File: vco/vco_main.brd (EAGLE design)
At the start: 94.9 x 107.9 mm, 82 parts, among them IC1 OPA4130U, IC2 LM13700M, IC3 OPA4130U, IC4 OPA4130U, Q1 MMBFJ3

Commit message: added gerbers
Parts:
- added C10, C11, C12, C13, C14, C15, C16, C17, C18, C19, C8, C9: 1n, dan:C0603
- moved R13 12.0 mm to (15.2, 95.2)
- moved U$2 5.08 mm to (8.89, 49.5)
- moved Q1 2.84 mm to (87.6, 76.2)
- moved C1 1.27 mm to (15.2, 85.1), turned to 270 degrees
- moved R1 1.27 mm to (12.7, 85.1), turned to 90 degrees
- moved U$5 1.27 mm to (86.4, 97.8)
- turned C7 to 270 degrees
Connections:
- net +12V: now also C14.1, C15.1, C16.1, C17.1, C18.1, C19.1, IC2.11, POWER.10, POWER.9
- net -12V: now also C10.1, C11.1, C12.1, C13.1, C8.1, C9.1, IC2.6, POWER.1, POWER.2
- net GND: now also C10.2, C11.2, C12.2, C13.2, C14.2, C15.2, C16.2, C17.2, C18.2, C19.2, C8.2, C9.2, POWER.3, POWER.4, POWER.5, POWER.6, POWER.7, POWER.8
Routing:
- net -12V: track 0.00 -> 289.4 mm, vias 0 -> 21
- net +12V: track 0.00 -> 244.0 mm, vias 0 -> 18
- net SYNC: track 0.00 -> 228.2 mm, vias 0 -> 13
- net N$5: track 2.54 -> 185.8 mm, vias 0 -> 18
- net TRI: track 2.54 -> 163.4 mm, vias 0 -> 15
- net N$12: track 0.00 -> 145.1 mm, vias 0 -> 11
- net N$4: track 0.00 -> 138.5 mm, vias 0 -> 12
- net N$36: track 0.00 -> 128.6 mm, vias 0 -> 7
- net N$50: track 0.00 -> 120.6 mm, vias 0 -> 7
- net N$9: track 0.00 -> 118.5 mm, vias 0 -> 8
- net N$19: track 0.00 -> 112.2 mm, vias 0 -> 5
- net N$3: track 0.00 -> 107.4 mm, vias 0 -> 12
- net N$45: track 0.00 -> 103.5 mm, vias 0 -> 5
- net N$24: track 0.00 -> 102.9 mm, vias 0 -> 5
- net N$51: track 0.00 -> 83.0 mm, vias 0 -> 6
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- added copper zone on layer 16, net GND
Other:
- board size 94.9 x 107.9 mm -> 94.9 x 108 mm
- board text added: "tempco"

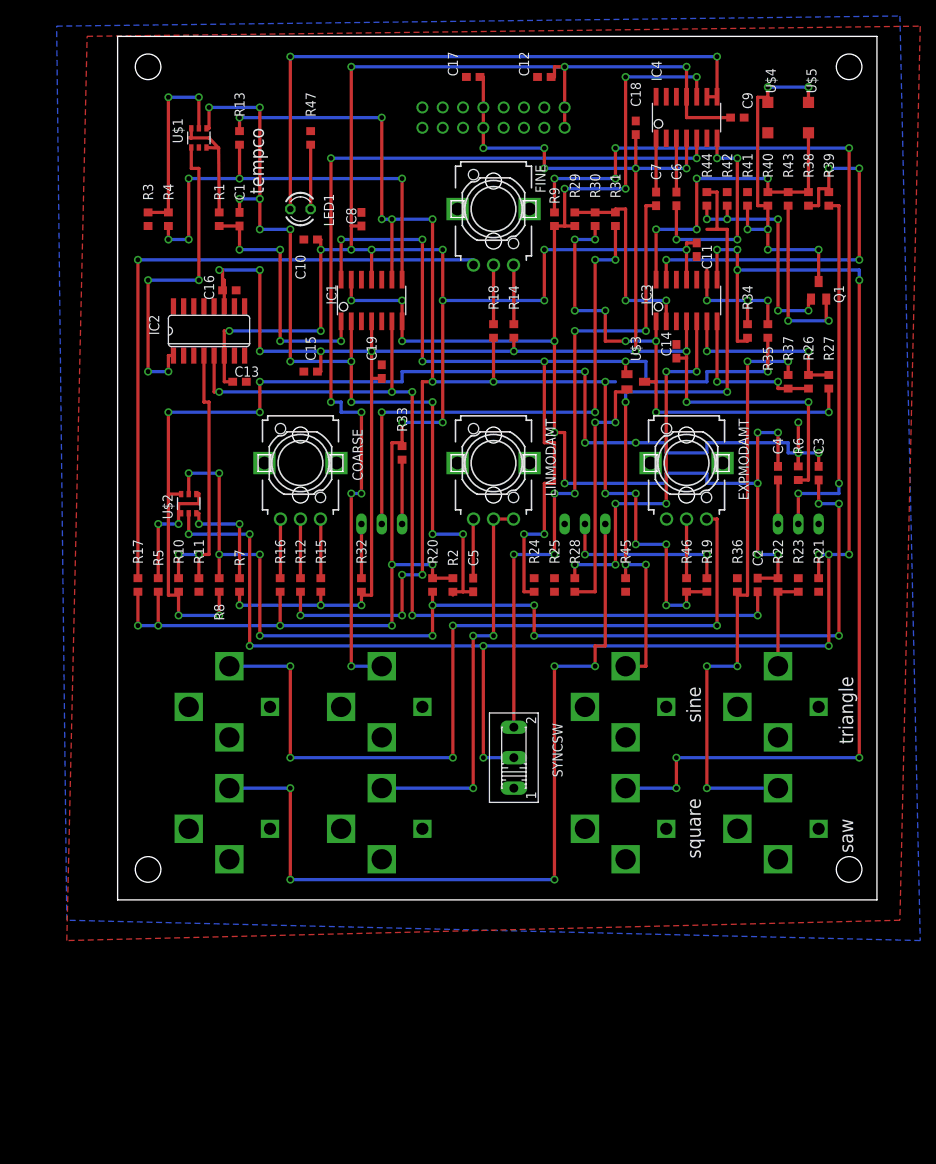
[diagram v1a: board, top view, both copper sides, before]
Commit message: fixed the schematic.  need to check polarity on current source and square comparator.  moved most of the labels to the silkscreen layer, but need to do that with the new components.
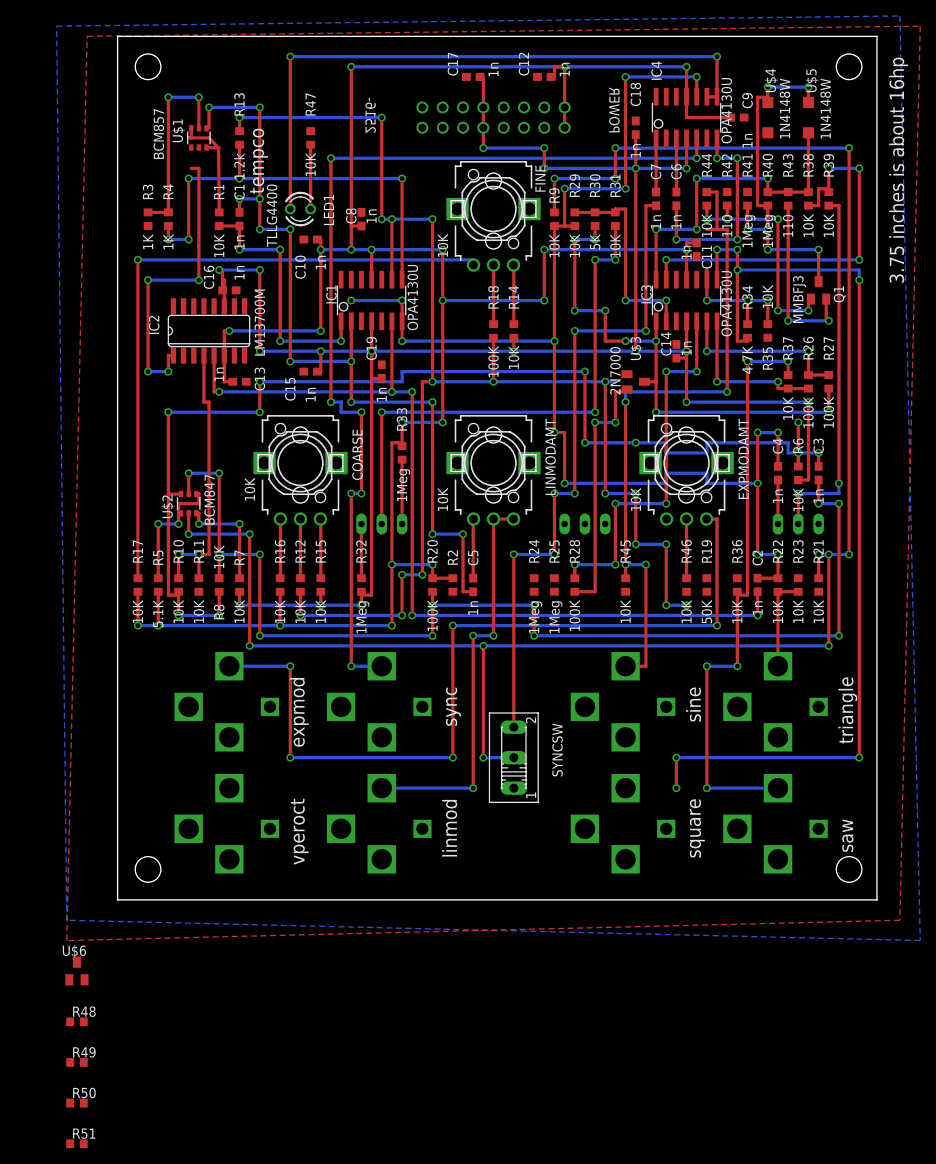
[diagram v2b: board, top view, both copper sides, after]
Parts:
- added R48: 4.7K, dan:R0603
- added R49, R50, R51: 10K, dan:R0603
- added U$6: MMBT3904, dan:SOT23
- R13: value 10K -> 1.2k
- R18, R26, R27, R28: value 10K -> 100K
- R19: value 10K -> 50K
- R2: value (none) -> 1Meg
- R3, R4: value 10K -> 1K
- R30: value 10K -> 5K
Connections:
- removed net IABC1: IC2.1, U$1.4
- new net IABC: IC2.1, U$1.1
- new net N$54: IC4.12, VPEROCT.P$3
- new net N$55: IC4.13, IC4.14, SCALE.E
- new net N$56: SCALE.S, U$6.1
- new net N$58: R51.1
- new net N$9: R49.2, R50.1, SQUARE.P$3
- net +12V: now also U$6.3
- net -12V: now also R48.1
- net GND: now also IC1.13, R50.2; no longer IC1.12, LINMOD.P$2
- net N$22: now also R48.2, U$6.2; no longer SCALE.S
- net N$24: now also R2.2, U$1.4; no longer SCALE.E, VPEROCT.P$3
- net N$3: no longer R2.2, U$1.1
- net N$36: now also R49.1; no longer SQUARE.P$3
- net TRI: now also IC1.12, R51.2; no longer IC1.13
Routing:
- net N$57: track 118.5 -> 0.00 mm, vias 8 -> 0
- net N$24: track 102.9 -> 0.00 mm, vias 5 -> 0
- net IABC1: track 40.5 -> 0.00 mm, vias 4 -> 0
- net IABC: track 0.00 -> 37.9 mm, vias 0 -> 4
- net N$22: track 22.0 -> 0.00 mm, vias 2 -> 0
- net N$36: track 128.6 -> 122.3 mm
- net N$5: track 185.8 -> 181.5 mm
- net TRI: track 163.4 -> 160.8 mm
- net N$3: track 107.4 -> 105.4 mm

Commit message: fixed schematic.  moved all labels to silkscreen.  fixed layout.  need to make gerbers.
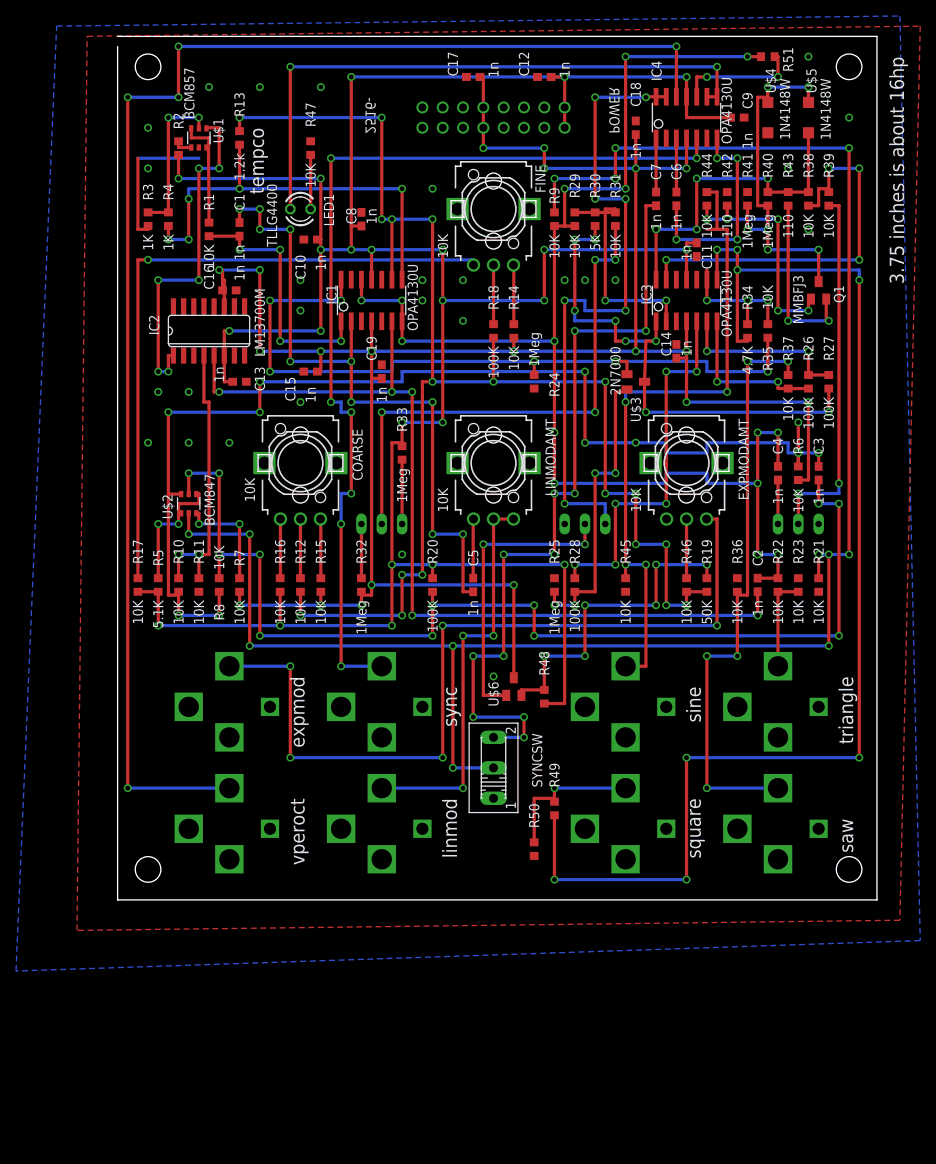
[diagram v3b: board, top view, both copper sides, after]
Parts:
- moved R51 161.0 mm to (81.3, 105.4)
- moved R48 71.2 mm to (53.3, 25.4), turned to 90 degrees
- moved R49 67.6 mm to (54.6, 11.4), turned to 90 degrees
- moved R50 65.4 mm to (52.1, 6.35), turned to 270 degrees
- moved U$6 65.2 mm to (49.5, 26.7)
- moved R2 64.5 mm to (7.62, 94.0), turned to 90 degrees
- moved R24 25.4 mm to (52.1, 64.8), turned to 90 degrees
- moved SYNCSW 2.84 mm to (47.0, 16.5)
- moved R1 1.80 mm to (11.4, 83.8)
- moved C1 1.27 mm to (15.2, 83.8)
- moved R47 1.27 mm to (24.1, 94.0)
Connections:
- removed net N$58: R51.1
- new net N$59: IC4.10, R51.2
- net TRI: now also R51.1; no longer IC4.10, R51.2
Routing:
- net N$54: track 0.00 -> 180.3 mm, vias 0 -> 5
- net N$57: track 0.00 -> 94.1 mm, vias 0 -> 6
- net N$55: track 0.00 -> 81.3 mm, vias 0 -> 7
- net -12V: track 289.4 -> 342.3 mm, vias 21 -> 23
- net N$22: track 0.00 -> 41.2 mm, vias 0 -> 6
- net N$56: track 0.00 -> 37.0 mm, vias 0 -> 2
- net N$36: track 122.3 -> 157.0 mm, vias 7 -> 8
- net +12V: track 244.0 -> 273.3 mm, vias 18 -> 20
- net N$3: track 105.4 -> 83.8 mm, vias 12 -> 10
- net N$9: track 0.00 -> 19.0 mm, vias 0 -> 1
- net GND: track 0.00 -> 18.2 mm, vias 0 -> 27
- net N$51: track 83.0 -> 99.5 mm, vias 6 -> 11
- net N$59: track 0.00 -> 15.6 mm, vias 0 -> 2
- net TRI: track 160.8 -> 170.2 mm
- net N$10: track 31.8 -> 37.7 mm, vias 2 -> 4
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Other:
- board size 94.9 x 108 mm -> 94.9 x 107.9 mm

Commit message: fixed some drc errors.  made gerbers.  silkscreen gerber doesn't seem to be getting the fonts correctly.
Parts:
- added R52: 1Meg, dan:R0603
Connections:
- net GND: now also R52.1
- net N$54: now also R52.2
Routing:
- net GND: track 18.2 -> 8.04 mm
- net N$54: track 180.3 -> 185.4 mm

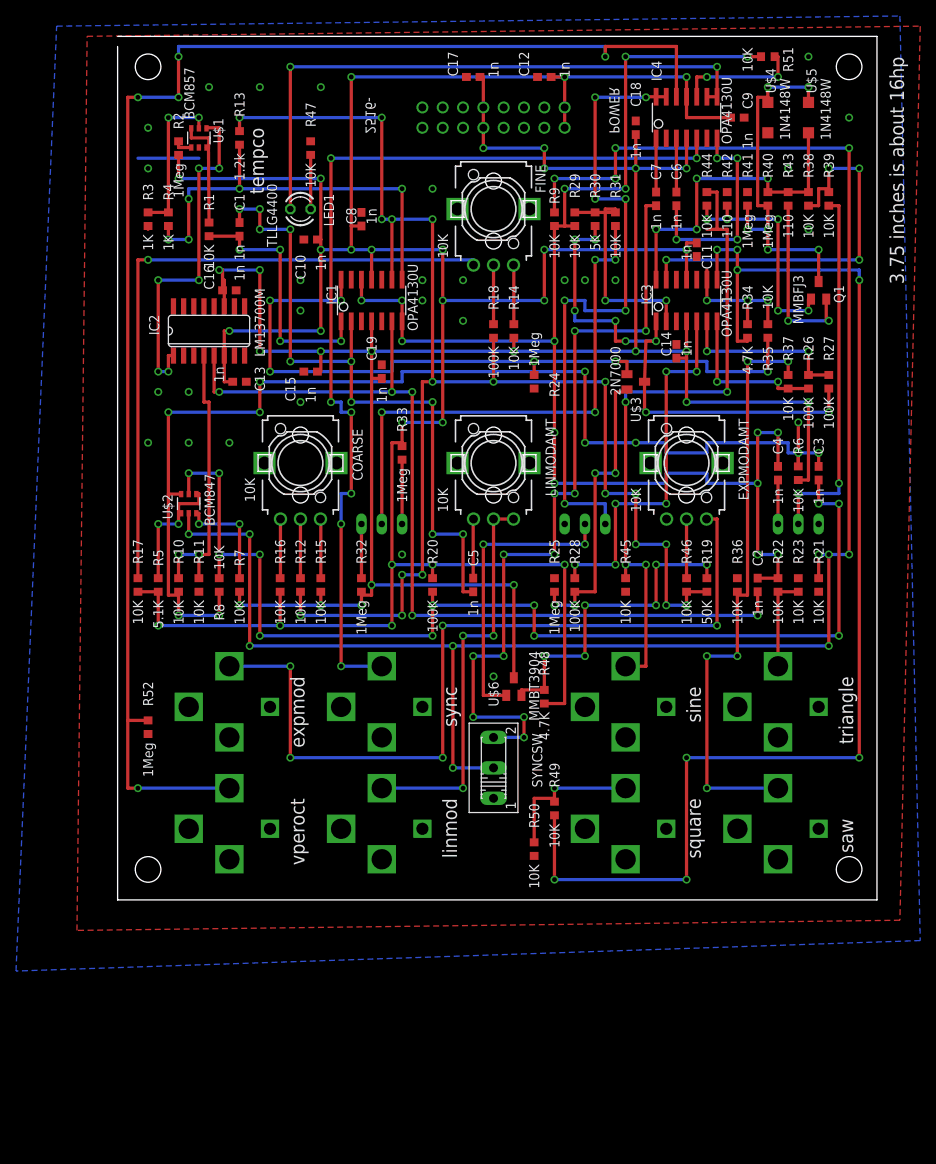
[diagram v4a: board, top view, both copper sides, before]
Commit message: fixed silkscreen.  fixed linear mod.  started to think about critical nets.
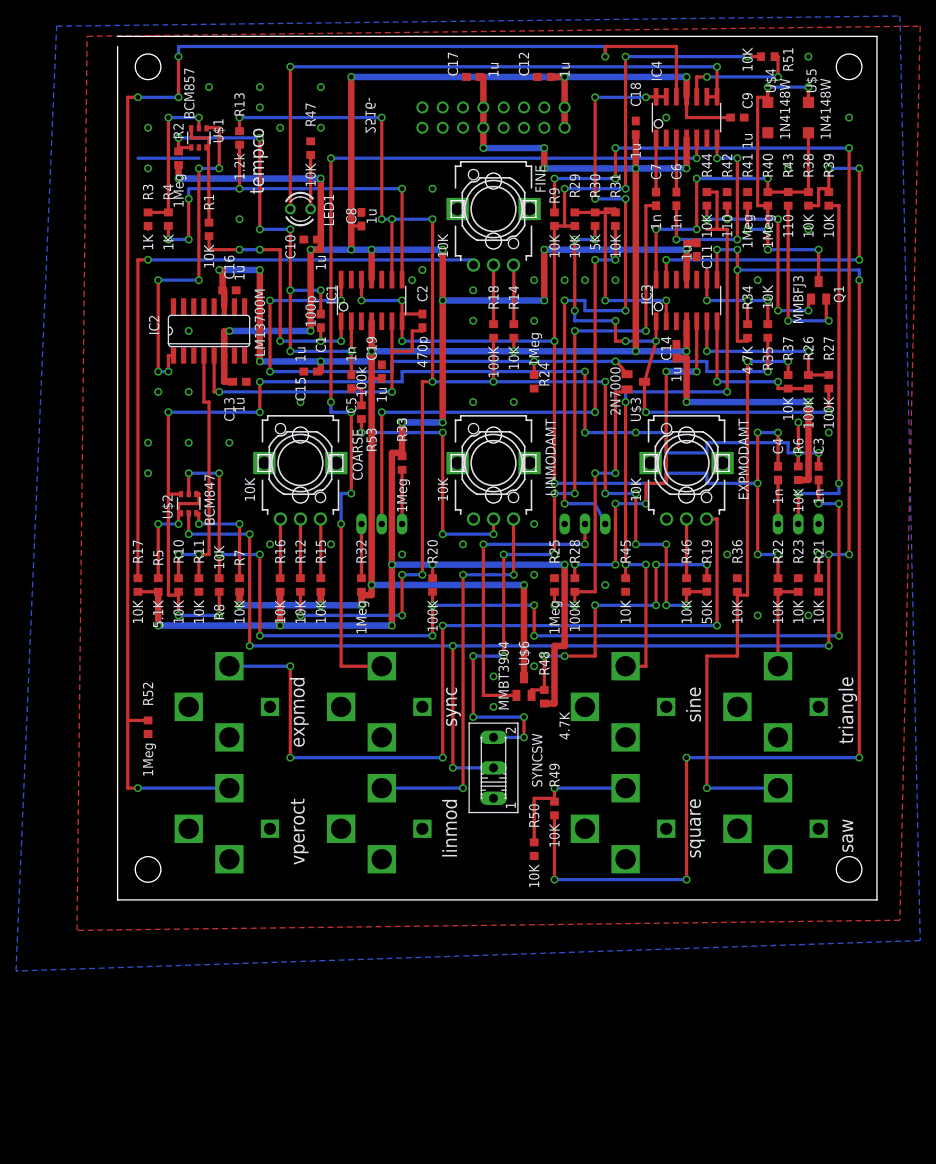
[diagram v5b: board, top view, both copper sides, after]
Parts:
- added R53: 100k, dan:R0603
- C1: value 1n -> 100p
- C10, C11, C12, C13, C14, C15, C16, C17, C18, C19, C8, C9: value 1n -> 1u
- C2: value 1n -> 470p
- moved C2 53.4 mm to (38.1, 72.4)
- moved C5 29.6 mm to (29.2, 64.8), turned to 270 degrees
- moved C1 15.3 mm to (25.4, 72.4)
- moved R2 1.27 mm to (7.62, 92.7)
- moved R33 1.27 mm to (35.6, 54.6)
- moved U$6 1.27 mm to (50.8, 26.7)
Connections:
- net GND: now also LINMODAMT.1
- net N$24: now also LINMOD.P$3, LINMODAMT.3; no longer R2.2, U$1.4
- net N$3: now also R2.2, U$1.4
- net N$46: now also R53.1; no longer LINMOD.P$3, LINMODAMT.3
- net N$48: now also R53.2; no longer LINMODAMT.1
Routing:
- net N$19: track 112.2 -> 42.4 mm, vias 5 -> 2
- net N$24: track 2.37 -> 50.2 mm, vias 0 -> 3
- net N$3: track 83.8 -> 65.0 mm, vias 10 -> 8
- net N$46: track 50.1 -> 32.8 mm, vias 3 -> 4
- net N$48: track 7.43 -> 3.38 mm
- net N$2: track 32.1 -> 33.8 mm, vias 4 -> 5
- net N$56: track 37.0 -> 38.3 mm
- net N$31: track 8.04 -> 6.77 mm
- net N$22: track 41.2 -> 39.9 mm
- net N$28: track 65.7 -> 64.6 mm
- net N$55: track 81.3 -> 80.4 mm
- net N$57: track 94.1 -> 93.3 mm
- net TRI: vias 15 -> 14
- net N$50: track 120.6 -> 120.7 mm, vias 7 -> 6
- net N$33: vias 5 -> 3
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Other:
- board text added: "RED"
- board text removed: "3.75 inches is about 16hp"

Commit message: fixed up the symmetry.  added a front panel.
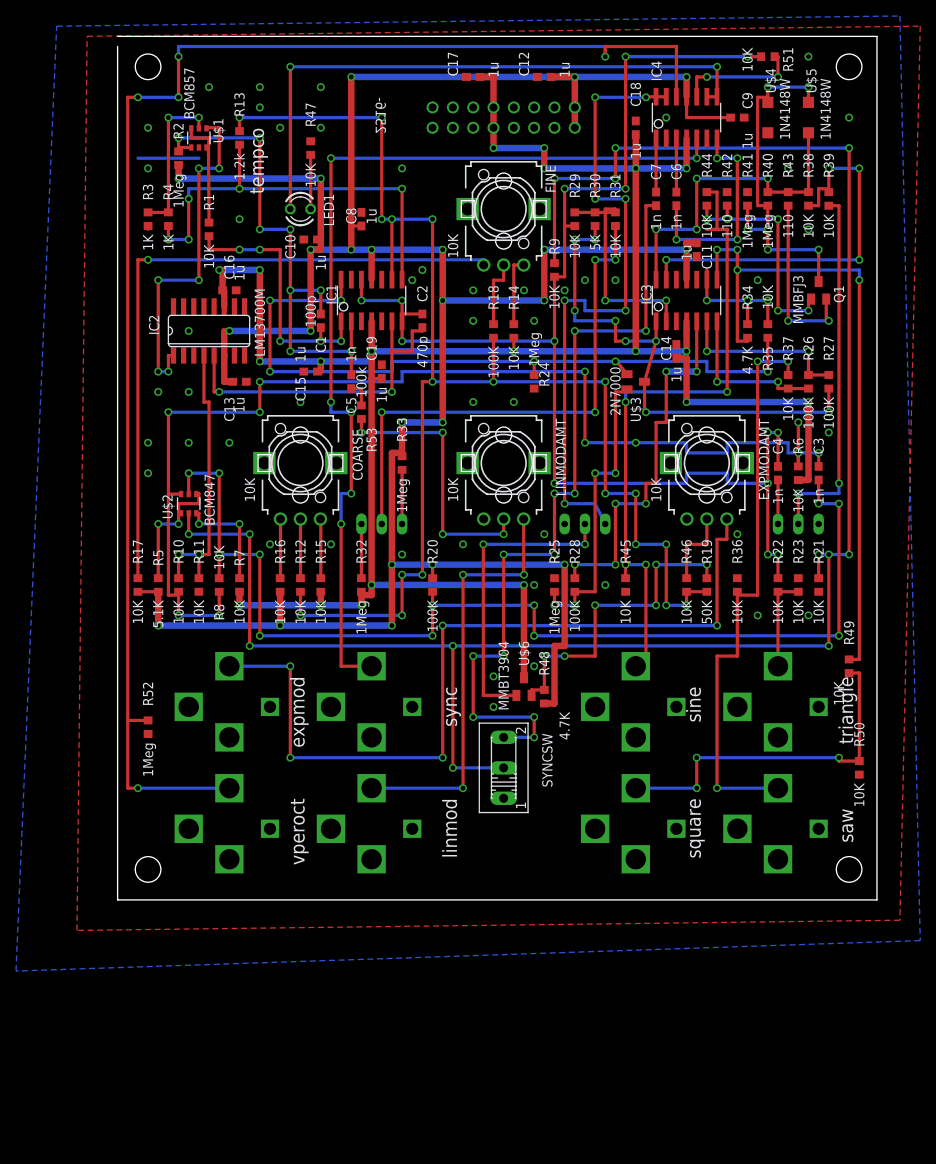
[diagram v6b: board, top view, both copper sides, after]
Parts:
- moved R50 41.9 mm to (92.7, 16.5)
- moved R49 40.9 mm to (91.4, 29.2), turned to 270 degrees
- moved R9 6.35 mm to (54.6, 78.7)
- moved EXPMODAMT 2.54 mm to (73.7, 54.6)
- moved LINMOD 1.27 mm to (31.8, 8.89)
- moved SYNC 1.27 mm to (31.8, 24.1)
- moved FINE 1.27 mm to (48.3, 86.4)
- moved LINMODAMT 1.27 mm to (48.3, 54.6)
- moved POWER 1.27 mm to (48.3, 97.8)
- moved SIN 1.27 mm to (64.8, 24.1)
- moved SQUARE 1.27 mm to (64.8, 8.89)
- moved SYNCSW 1.27 mm to (48.3, 16.5)
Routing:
- net N$36: track 157.0 -> 84.6 mm, vias 8 -> 4
- net N$9: track 19.0 -> 44.4 mm, vias 1 -> 3
- net SYNC: track 230.8 -> 238.4 mm
- net N$33: track 74.9 -> 72.4 mm
- net N$24: track 50.2 -> 52.7 mm
- net N$42: track 7.39 -> 9.93 mm
- net N$51: track 99.5 -> 100.8 mm
- net N$40: track 82.6 -> 81.3 mm
- net N$20: track 82.4 -> 83.7 mm
- net N$50: track 120.7 -> 119.4 mm
- net N$46: track 32.8 -> 34.1 mm
- net N$21: track 7.39 -> 8.66 mm
- net -12V: track 341.9 -> 343.2 mm
- net TRI: track 170.2 -> 169.0 mm
- net N$8: track 7.47 -> 8.62 mm
